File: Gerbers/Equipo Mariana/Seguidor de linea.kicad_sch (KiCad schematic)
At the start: 23 parts, among them J1 VCC, J11 I2C PROTOCOL, J2 MOTOR A, J3 MOTOR B, J4 Regleta_Jabots, J5 TURBIBNA, J7 Conn_02x01, SW1 SW_SPDT, U2 ESP32-DEVKIT-V1, U3 LM7805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

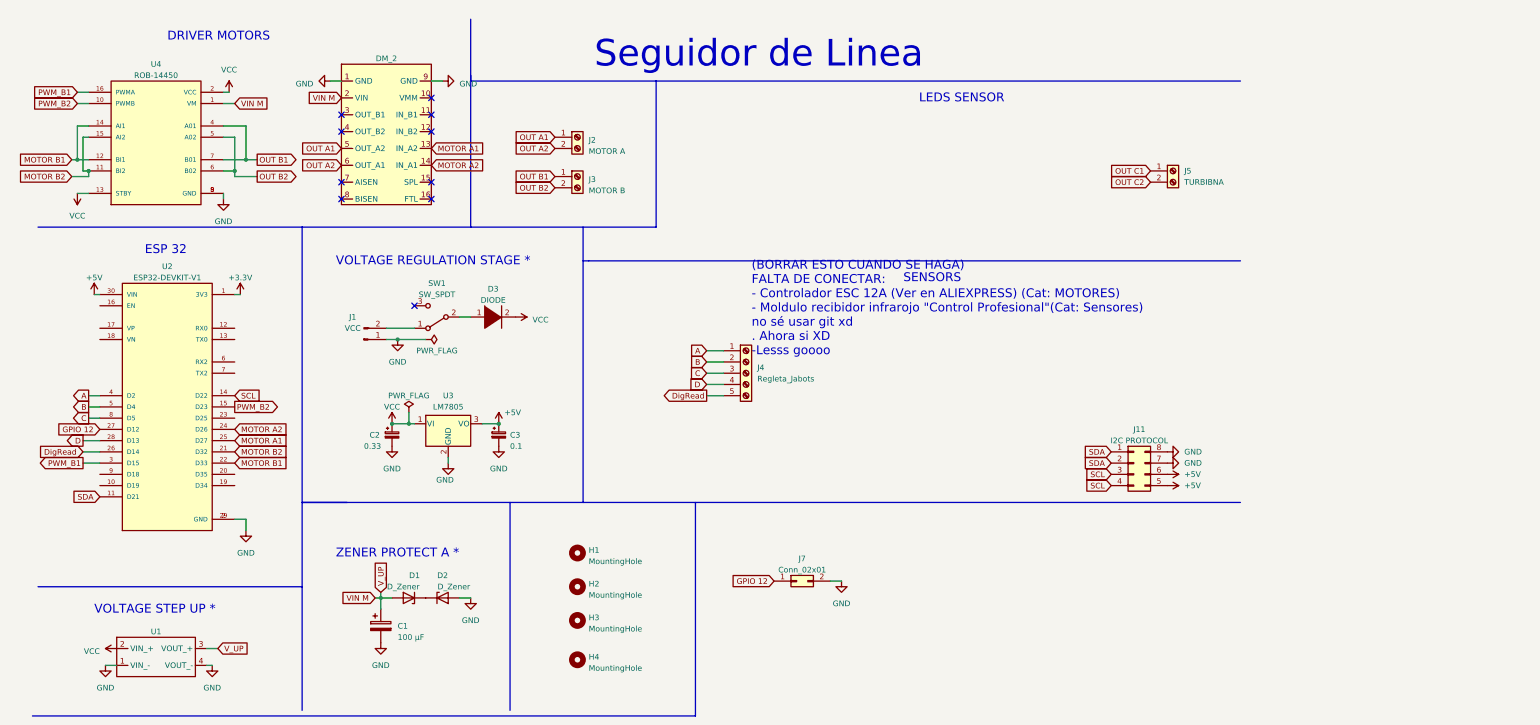
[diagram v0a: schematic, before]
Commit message: Segundo Driver de motor añadido
-Termine lo del segundo driver de motor
-Acomode el esquema
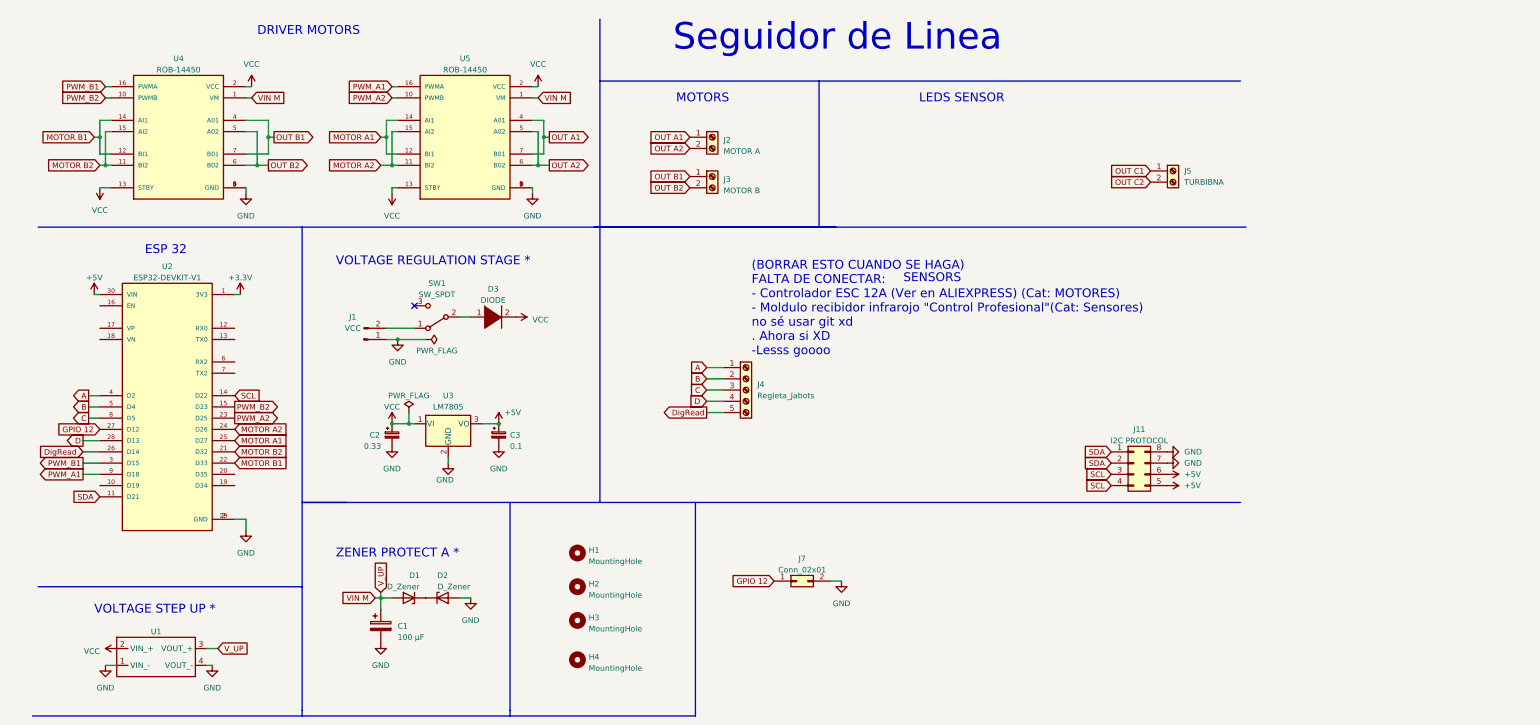
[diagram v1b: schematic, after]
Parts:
- removed DM_2: ~, DRV 8833:DRV 8833, symbol DRV 8833:DRV_8833
- added U5: ROB-14450, ROB-14450:MODULE_ROB-14450, symbol ROB-14450:ROB-14450
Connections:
- net GND: now also U5.3 (GND), U5.8 (GND), U5.9 (GND)
- net MOTOR A1: now also U5.12 (BI1), U5.14 (AI1)
- net MOTOR A2: now also U5.11 (BI2), U5.15 (AI2)
- net OUT A1: now also U5.4 (A01), U5.7 (B01)
- net OUT A2: now also U5.5 (A02), U5.6 (B02)
- net VCC: now also U5.13 (STBY), U5.2 (VCC)
- net VIN M: now also U5.1 (VM)
- net PWM_A2: now reaches U2.23 (D25)
- net PWM_A2: now also U5.10 (PWMB)
- net PWM_A1: now reaches U2.9 (D18)
- net PWM_A1: now also U5.16 (PWMA)
- no-connect marks 10 -> 1
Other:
- note added: "MOTORS"
- moved on the sheet: J2, J3, J4, U4

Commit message: Módulo start
Agregué el módulo de start a sensors, con un total de 3 pines para signal, VCC y Gnd
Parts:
- added GND: +5V, Connector_PinHeader_2.54mm:PinHeader_1x03_P2.54mm_Vertical, symbol Connector_Generic:Conn_01x03
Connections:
- net GND: now also GND.2 (Pin_2)
- net VCC: now also GND.3 (Pin_3)
- net SIGNAL: now reaches U2.10 (D19)
- net SIGNAL: now also GND.1 (Pin_1)
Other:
- note added: "Módulo de start"
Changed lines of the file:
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@@
     (effects (font (face "Rexlia") (size 2 2) (color 0 0 0 1)) (justify left bottom))
+  )
+  (text "Módulo de start" (at 207.01 95.25 0)
+    (effects (font (size 1.27 1.27)) (justify left bottom))
   )
   (text "Seguidor de Linea" (at 156.21 24.13 0)
@@
     (effects (font (size 1.27 1.27)) (justify right))
     (property "Intersheetrefs" "${INTERSHEET_REFS}" (at 254.0991 50.8 0)
+      (effects (font (size 1.27 1.27)) (justify right) hide)
+    )
+  )
+  (global_label "SIGNAL" (shape input) (at 210.82 99.06 180) (fields_autoplaced)
+    (effects (font (size 1.27 1.27)) (justify right))
+    (property "Intersheetrefs" "${INTERSHEET_REFS}" (at 201.3033 99.06 0)
       (effects (font (size 1.27 1.27)) (justify right) hide)
     )
@@
     )
   )
+  (global_label "SIGNAL" (shape input) (at 26.67 121.92 180) (fields_autoplaced)
+    (effects (font (size 1.27 1.27)) (justify right))
+    (property "Intersheetrefs" "${INTERSHEET_REFS}" (at 17.1533 121.92 0)
+      (effects (font (size 1.27 1.27)) (justify right) hide)
+    )
+  )
   (global_label "PWM_A2" (shape input) (at 92.71 34.29 180) (fields_autoplaced)
     (effects (font (size 1.27 1.27)) (justify right))
@@
         (path "/f4ce689f-74b7-4dbc-ad47-3301b8dc97a2"
           (reference "#PWR08") (unit 1)
+        )
+      )
+    )
+  )
+  (symbol (lib_name "GND_2") (lib_id "power:GND") (at 210.82 101.6 270) (unit 1)
+    (in_bom yes) (on_board yes) (dnp no) (fields_autoplaced)
+    (property "Reference" "#PWR025" (at 204.47 101.6 0)
+      (effects (font (size 1.27 1.27)) hide)
+    )
+    (property "Value" "GND" (at 207.01 101.6 90)
+      (effects (font (size 1.27 1.27)) (justify right))
+    )
+    (property "Footprint" "" (at 210.82 101.6 0)
+      (effects (font (size 1.27 1.27)) hide)
+    )
+    (property "Datasheet" "" (at 210.82 101.6 0)
+      (effects (font (size 1.27 1.27)) hide)
+    )
+    (pin "1")
+    (instances
+      (project "Seguidor de linea"
+        (path "/f4ce689f-74b7-4dbc-ad47-3301b8dc97a2"
+          (reference "#PWR025") (unit 1)
         )
       )
@@
         )
       )
+    )
+  )
+  (symbol (lib_name "VCC_3") (lib_id "power:VCC") (at 210.82 104.14 90) (unit 1)
+    (in_bom yes) (on_board yes) (dnp no) (fields_autoplaced)
+    (property "Reference" "#PWR024" (at 214.63 104.14 0)
+      (effects (font (size 1.27 1.27)) hide)
+    )
+    (property "Value" "VCC" (at 207.01 104.14 90)
+      (effects (font (size 1.27 1.27)) (justify left))
+    )
+    (property "Footprint" "" (at 210.82 104.14 0)
+      (effects (font (size 1.27 1.27)) hide)
+    )
+    (property "Datasheet" "" (at 210.82 104.14 0)
+      (effects (font (size 1.27 1.27)) hide)
+    )
+    (pin "1")
+    (instances
+      (project "Seguidor de linea"
+        (path "/f4ce689f-74b7-4dbc-ad47-3301b8dc97a2"
+          (reference "#PWR024") (unit 1)
+        )
+      )
+    )
+  )
+  (symbol (lib_id "Connector_Generic:Conn_01x03") (at 215.9 101.6 0) (unit 1)
+    (in_bom yes) (on_board yes) (dnp no)
+    (property "Reference" "GND" (at 218.44 100.33 0)
+      (effects (font (size 1.27 1.27)) (justify left))
+    )
+    (property "Value" "+5V" (at 218.44 102.87 0)
+      (effects (font (size 1.27 1.27)) (justify left))
+    )
+    (property "Footprint" "Connector_PinHeader_2.54mm:PinHeader_1x03_P2.54mm_Vertical" (at 215.9 101.6 0)
+      (effects (font (size 1.27 1.27)) hide)
+    )
+    (property "Datasheet" "~" (at 215.9 101.6 0)
+      (effects (font (size 1.27 1.27)) hide)
+    )
+    (pin "1")
+    (pin "2")
+    (pin "3")
+    (instances
+      (project "Seguidor de linea"
+        (path "/f4ce689f-74b7-4dbc-ad47-3301b8dc97a2"
+          (reference "GND") (unit 1)
+        )
+      )

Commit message: Update Seguidor de linea.kicad_sch
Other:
- note added: "(BORRAR ESTO CUANDO SE HAGA) FALTA DE CONECTAR: - Módulo recibidor infrarojo "Control Profesional"(Cat: Sensores) - Ya está el módulo de start de 3 pines conectados como salidas y a la ESP32 como entradas"
- note removed: "(BORRAR ESTO CUANDO SE HAGA) FALTA DE CONECTAR: - Controlador ESC 12A (Ver en ALIEXPRESS) (Cat: MOTORES) - Moldulo recibidor infrarojo "Control Profesional"(Cat: Sensores) no sé usar git xd . Ahora si XD -Lesss goooo"
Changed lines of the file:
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@@
     (effects (font (size 6 6) (color 0 0 0 1)) (justify left bottom))
   )
-  (text "(BORRAR ESTO CUANDO SE HAGA)\nFALTA DE CONECTAR:\n- Controlador ESC 12A (Ver en ALIEXPRESS) (Cat: MOTORES)\n- Moldulo recibidor infrarojo \"Control Profesional\"(Cat: Sensores)\nno sé usar git xd\n. Ahora si XD\n-Lesss goooo\n"
+  (text "(BORRAR ESTO CUANDO SE HAGA)\nFALTA DE CONECTAR:\n- Módulo recibidor infrarojo \"Control Profesional\"(Cat: Sensores)\n- Ya está el módulo de start de 3 pines conectados como salidas y a la ESP32 como entradas\n\n"
     (at 173.99 92.71 0)
     (effects (font (size 2 2) (color 0 0 0 1)) (justify left bottom))
